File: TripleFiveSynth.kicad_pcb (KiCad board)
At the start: 4 copper layers, 70.5 x 38 mm, 133 parts, among them J101 Conn_02x26_Odd_Even, Q1001 MMBT3904, Q1002 BSS84, Q1101 MMBT3904, Q1102 BSS84, Q1201 MMBT3904, Q1202 BSS84, Q1301 MMBT3904, Q1302 BSS84, Q201 MMBT3904, Q202 BSS84, Q301 MMBT3904, Q302 BSS84, Q401 MMBT3904, Q402 BSS84, Q501 MMBT3904, Q502 BSS84, Q601 MMBT3904, Q602 BSS84, Q701 MMBT3904, Q702 BSS84, Q801 MMBT3904, Q802 BSS84, Q901 MMBT3904, Q902 BSS84, U1001 NE555D, U1101 NE555D, U1201 NE555D, U1301 NE555D, U201 NE555D, U301 NE555D, U401 NE555D, U501 NE555D, U601 NE555D, U701 NE555D, U801 NE555D, U901 NE555D

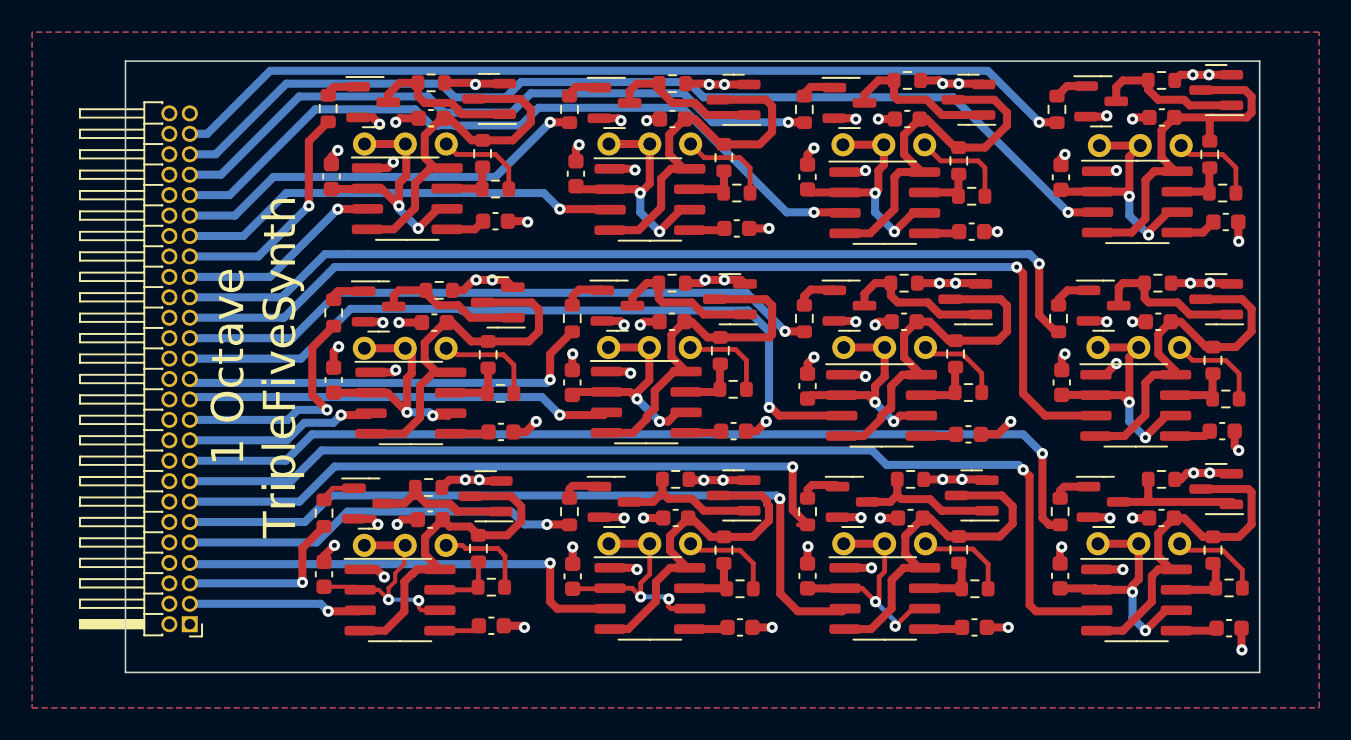
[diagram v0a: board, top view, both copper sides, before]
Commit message: swap to SMD Bourns 3224W, can stack in Eurorack now
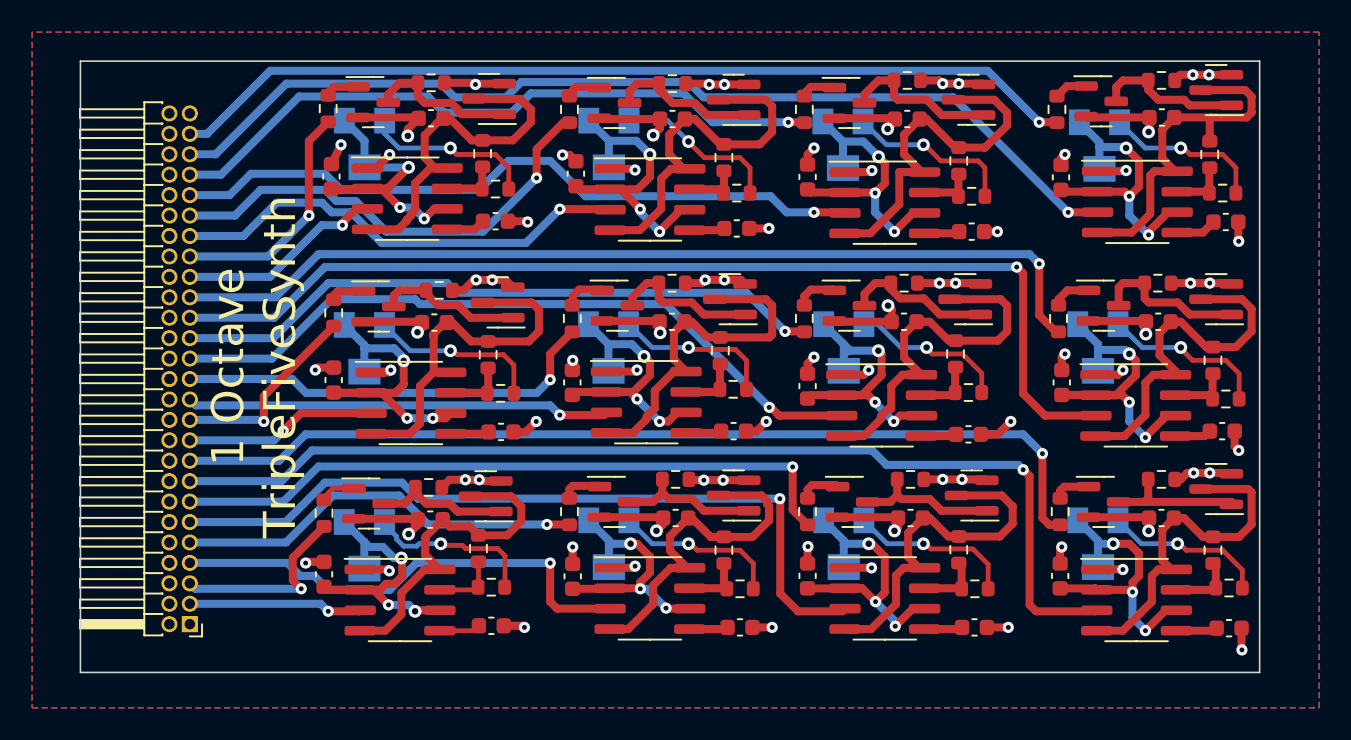
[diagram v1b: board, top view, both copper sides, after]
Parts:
- TR1001, TR1101, TR1201, TR1301, TR201, TR301, TR401, TR501, TR601, TR701, TR801, TR901: footprint Potentiometer_THT:Potentiometer_Bourns_3296W_Vertical -> TripleFiveSynth:Potentiometer_Bourns_3224W_Vertical
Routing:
- net GND: track 79.2 -> 106.1 mm, vias 60 -> 48
- net Net-(R504-Pad1): track 6.11 -> 11.0 mm, vias 0 -> 1
- net Net-(R904-Pad1): track 5.82 -> 10.7 mm, vias 0 -> 1
- net Net-(R404-Pad1): track 5.95 -> 10.6 mm, vias 0 -> 1
- net /Voice4/TR: track 14.2 -> 18.9 mm, vias 2 -> 3
- net Net-(R1204-Pad1): track 5.55 -> 10.2 mm, vias 0 -> 1
- net Net-(R604-Pad1): track 5.36 -> 9.93 mm, vias 0 -> 1
- net Net-(R804-Pad1): track 5.94 -> 10.5 mm, vias 0 -> 1
- net Net-(R1104-Pad1): track 5.88 -> 10.3 mm, vias 0 -> 1
- net Net-(R1004-Pad1): track 6.11 -> 10.5 mm, vias 0 -> 1
- net Net-(R204-Pad1): track 5.95 -> 10.4 mm, vias 0 -> 1
- net Net-(R304-Pad1): track 5.98 -> 10.4 mm, vias 0 -> 1
- net Net-(R1304-Pad1): track 5.69 -> 10.1 mm, vias 0 -> 1
- net Net-(R704-Pad1): track 5.63 -> 10.1 mm, vias 0 -> 1
- net /Voice6/TR: track 14.2 -> 18.5 mm, vias 2 -> 3
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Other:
- board size 70.5 x 38 mm -> 73.3 x 38 mm

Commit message: update with 5V and on-board sum
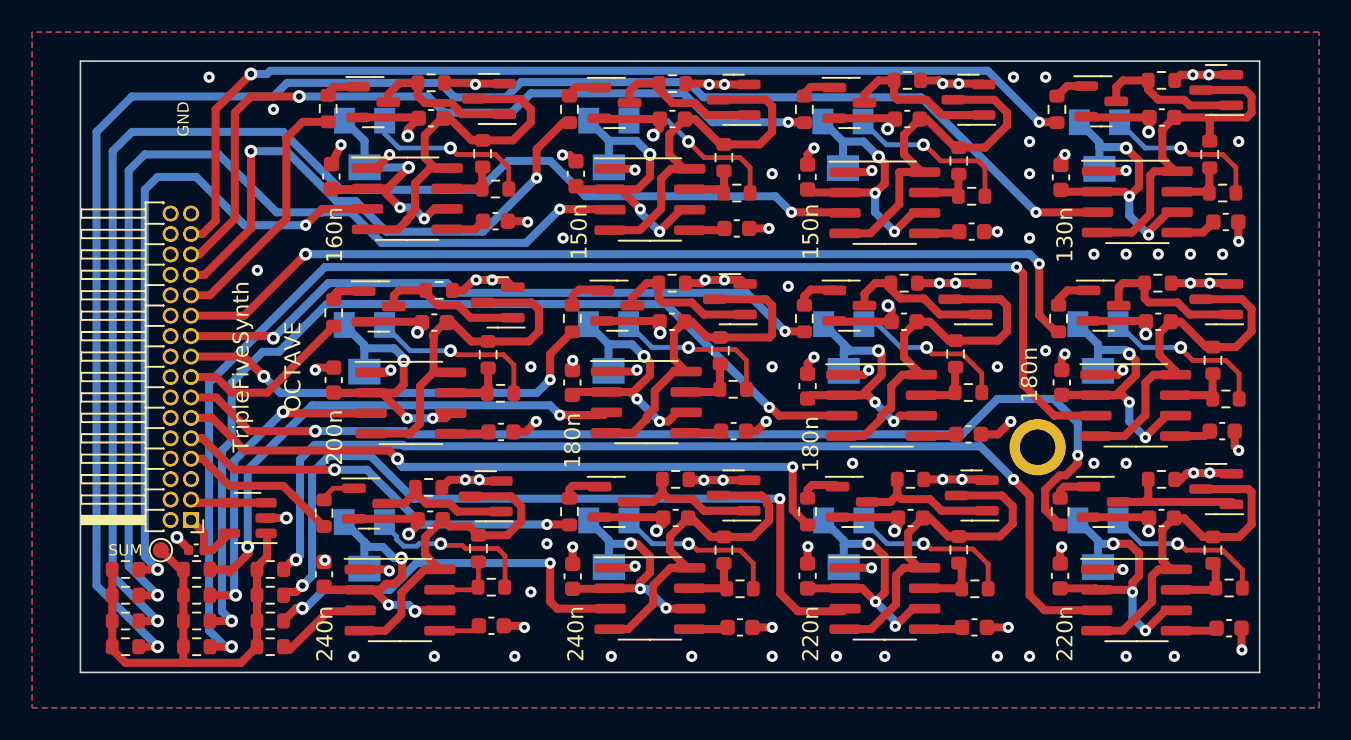
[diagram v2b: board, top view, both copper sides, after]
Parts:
- added C101: 100n, Capacitor_SMD:C_0402_1005Metric, F.Cu at (40.4, 59.4)
- added H101: MountingHole_Pad, MountingHole:MountingHole_2.2mm_M2_ISO7380_Pad, F.Cu at (92.7, 53.0)
- added R101: 10k, Resistor_SMD:R_0603_1608Metric, F.Cu at (45.0, 65.4)
- added R102: 10k, Resistor_SMD:R_0603_1608Metric, F.Cu at (45.0, 63.8)
- added R103: 10k, Resistor_SMD:R_0603_1608Metric, F.Cu at (45.0, 62.2)
- added R104: 10k, Resistor_SMD:R_0603_1608Metric, F.Cu at (45.0, 60.6)
- added R105: 10k, Resistor_SMD:R_0603_1608Metric, F.Cu at (40.4, 62.2)
- added R106: 10k, Resistor_SMD:R_0603_1608Metric, F.Cu at (40.4, 60.6)
- added R107: 10k, Resistor_SMD:R_0603_1608Metric, F.Cu at (40.4, 63.8)
- added R108: 10k, Resistor_SMD:R_0603_1608Metric, F.Cu at (40.4, 65.4)
- added R109: 10k, Resistor_SMD:R_0603_1608Metric, F.Cu at (36.0, 60.6)
- added R110: 10k, Resistor_SMD:R_0603_1608Metric, F.Cu at (36.0, 62.2)
- added R111: 10k, Resistor_SMD:R_0603_1608Metric, F.Cu at (36.0, 63.8)
- added R112: 10k, Resistor_SMD:R_0603_1608Metric, F.Cu at (36.0, 65.4)
- added TP101: SUM, TestPoint:TestPoint_Pad_D1.0mm, F.Cu at (38.2, 59.4)
- added U101: LMV321, Package_TO_SOT_SMD:SOT-23-5, F.Cu at (43.6, 57.4)
- J101: value Conn_02x26_Odd_Even -> OctaveIO; footprint Connector_PinHeader_1.27mm:PinHeader_2x26_P1.27mm_Horizontal -> Connector_PinHeader_1.27mm:PinHeader_2x16_P1.27mm_Horizontal
- moved J101 6.48 mm to (40.1, 57.5)
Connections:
- J101 pad 1: +12V -> +5V
- J101 pad 11: /OUTD -> /GATED
- J101 pad 13: /GATED -> /GATEDS
- J101 pad 15: /OUTDS -> /GATEE
- J101 pad 17: /GATEDS -> /GATEF
- J101 pad 19: /OUTE -> /GATEFS
- J101 pad 2: +12V -> +5V
- J101 pad 21: /GATEE -> /GATEG
- J101 pad 23: /OUTF -> /GATEGS
- J101 pad 25: /GATEF -> /GATEA
- J101 pad 27: /OUTFS -> /GATEAS
- J101 pad 29: /GATEFS -> /GATEB
- J101 pad 3: /OUTC -> /OUTSUM
- J101 pad 31: /OUTEG -> +5V
- J101 pad 32: GND -> +5V
- J101 pad 5: /GATEC -> GND
- J101 pad 7: /OUTCS -> /GATEC
- Q1002 pad 2: +12V -> +5V
- Q1102 pad 2: +12V -> +5V
- Q1202 pad 2: +12V -> +5V
- Q1302 pad 2: +12V -> +5V
- Q202 pad 2: +12V -> +5V
- Q302 pad 2: +12V -> +5V
- Q402 pad 2: +12V -> +5V
- Q502 pad 2: +12V -> +5V
- Q602 pad 2: +12V -> +5V
- Q702 pad 2: +12V -> +5V
- Q802 pad 2: +12V -> +5V
- Q902 pad 2: +12V -> +5V
- R1002 pad 1: +12V -> +5V
- R1102 pad 1: +12V -> +5V
- R1202 pad 1: +12V -> +5V
- R1302 pad 1: +12V -> +5V
- R202 pad 1: +12V -> +5V
- R302 pad 1: +12V -> +5V
- R402 pad 1: +12V -> +5V
- R502 pad 1: +12V -> +5V
- R602 pad 1: +12V -> +5V
- R702 pad 1: +12V -> +5V
- R802 pad 1: +12V -> +5V
- R902 pad 1: +12V -> +5V
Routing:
- net +5V: track 0.00 -> 51.0 mm, vias 0 -> 23
- net +12V: track 46.8 -> 0.00 mm, vias 23 -> 0
- net /OUTB: track 62.3 -> 102.4 mm, vias 1 -> 2
- net /OUTAS: track 43.8 -> 81.1 mm, vias 1 -> 2
- net /OUTA: track 28.9 -> 61.8 mm, vias 1 -> 2
- net /SUM: track 0.00 -> 30.0 mm
- net /OUTGS: track 12.9 -> 40.9 mm, vias 1 -> 2
- net /OUTEG: track 65.8 -> 84.5 mm, vias 1 -> 2
- net /OUTFS: track 45.1 -> 59.5 mm, vias 1 -> 2
- net /OUTE: track 12.0 -> 24.2 mm, vias 1 -> 2
- net /GATEB: track 56.9 -> 63.4 mm, vias 1 -> 2
- net /GATEA: track 29.2 -> 35.4 mm, vias 1 -> 2
- net /OUTF: track 26.4 -> 32.4 mm, vias 1 -> 2
- net /GATEDS: track 59.5 -> 65.4 mm, vias 1 -> 2
- net /GATEAS: track 41.9 -> 47.7 mm, vias 1 -> 2
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- added copper zone on In2.Cu, net +5V
- removed copper zone on In2.Cu, net +12V
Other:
- board text added: "GND"
- board text added: "TripleFiveSynth OCTAVE"
- board text removed: "1 Octave TripleFiveSynth"
